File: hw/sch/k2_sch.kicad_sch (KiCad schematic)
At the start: 0 parts

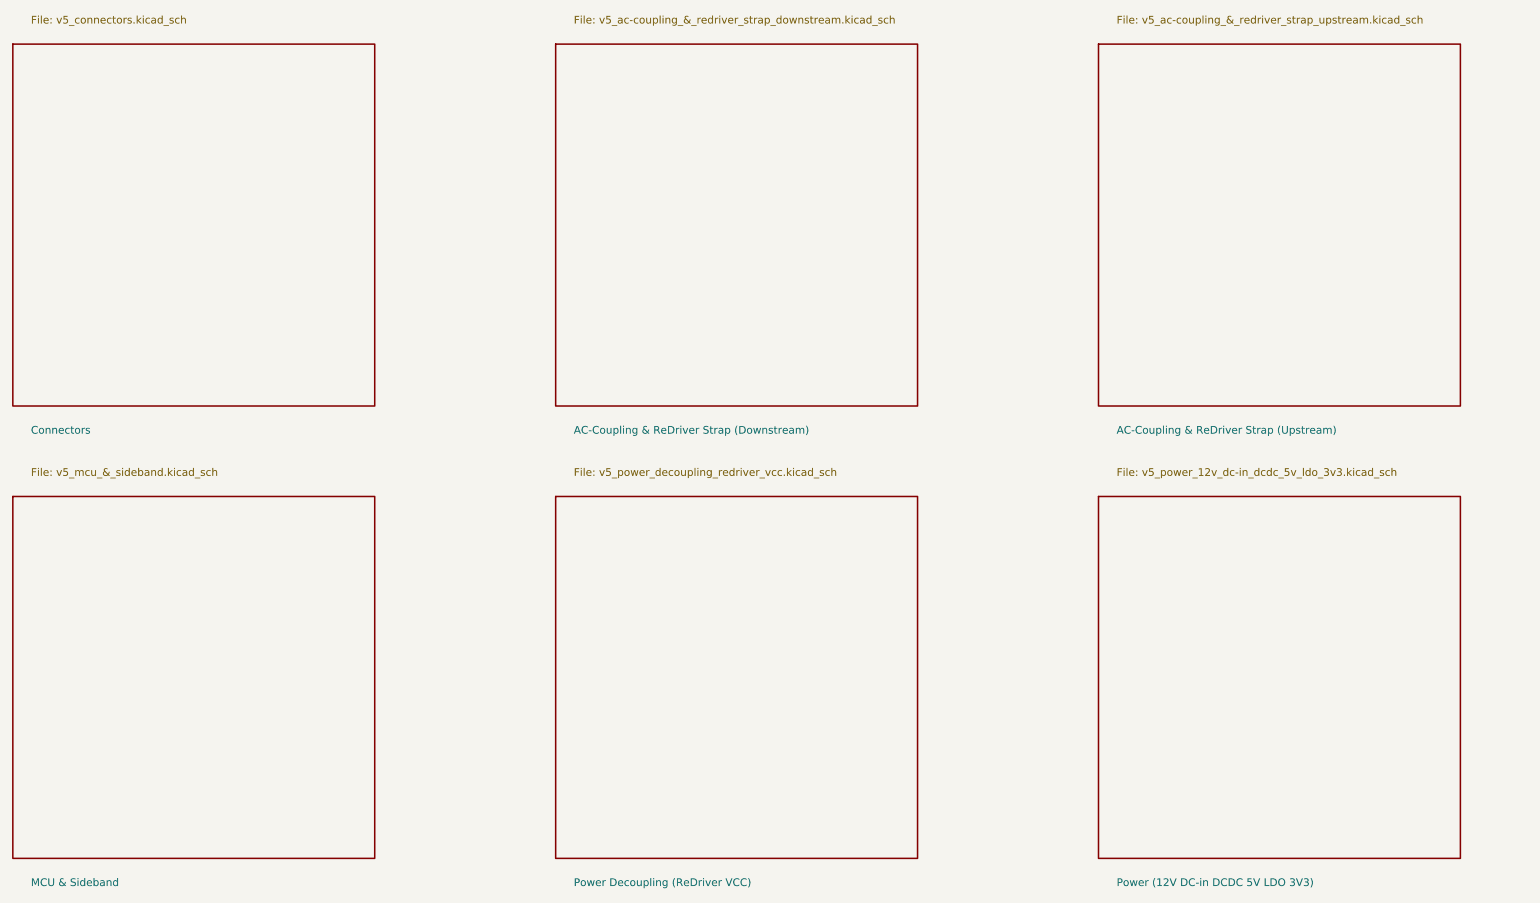
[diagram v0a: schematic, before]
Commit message: p2(k2): #K2-13 五问全落地 —— rev-21 + S2 纸张 A0 + S3 PWR_FLAG + R1/R2 安装 + §五 G1–G8 + E4
一、U1/S1：SPEC rev-21（d46bd017aa560716）
  = rev-20 − anchor_fixes.C64/C66（引 R1 分类留痕：C64=A1 耦合内置 / C66=D 类 VREG 域不存在）
  + spec_version 1.1.spec-rev-21 + _spec_rev_11 溯源卡 + anchor_fixes_removed_v21 留痕。
  机器证明：唯一值变 = spec_version；唯一删除 = C64/C66 六叶子；其余逐字节承 rev-20。
  rev-19/rev-20 原件未改；project.yaml 重指向；L3 README-canonical 同步。

二、S2：k2_sch.yaml 该 sheet paper A2→A0（逐字节 diff 仅 1 行；未采 (b)/(c)）。

三、S3：采纳 (a) —— driver 内 P9 通用规则「有 power_in 且无 power_out 的网各加 1 个虚拟
  PWR_FLAG（in_bom no / on_board no）」，参考号 #FLG01（避免 KiCad 批注错误导出告警）。
  实测命中网 = ['GND']；未改真源引脚类型；(b) 未采用。ERC error = 0。

四、安装（接受重排；原件留档）：写 5 件新 sheet + 覆写 root 与 IOCONVERT.kicad_sym；
  旧 6 件 v5_* 以 git mv 入 hw/sch/archive/（未删）。入 archive/ 系必要处置——判据侧
  measure_sch_refdes() glob 顶层 *.kicad_sch，且 _EXCL 视 /archive/ 为归档，否则 E1 被 6L 旧件污染。
  映射表 + 新 canonical 集合与 sha 见 hw/sch/README-canonical.md（#K2-13 §二.2 禁静默）。

五、落盘后机检
  C1 确定性 PASS（两次连跑逐字节同）
  T1 PASS：退役名 *_U3/_U7 = ∅；32/32 保留名并网且球映射与 T3 表一致
    （PCIe_DN_OUT0_P_MCIO→J3/3 + U6 M26=A_PETP0；UP0_P_J2→J2/2 + U6 P10=B_PETP0）
  T2 留痕：R4/R9/R26/R27 未出现在再生图（真源不含），删据 = 冻结 SPEC strap_domain_v32
    （ALL_DONE/READ_EN = NC no-action）+ R1 C 类；以文档留痕替代编辑级图注（(ii) 不产编辑注）
  E1 复算：板 42 / 图 55 / 网表 55；板-图 = 0；图-板 = 13 = P4 补件（按 O2 登记，非不一致）
  E4 PASS：两次 sha 同（k2_v6.kicad_pcb f615ffe6b83b88a3）+ refs 42 + 边框 120×46mm + 自检 6/6
  ERC：error 0；warning 豁免登记（452 off-grid 真源几何 / 55 lib + 15 footprint 环境 /
    1 lib_symbol_mismatch = PWR_FLAG 内嵌定义）

六、§五 G1–G8 落仓内生成器（k2/tools/k2_gen_v5.py）：板框 46mm、SPEC 经 pm_gate.config（自定位）、
  K2_REFS 由真源板导出、OLD_REF_MAP 与 pad65 特判移除、AC 检查/S7/capacitor_walls 段移除
  （保留 anchor_fixes 严格校验）；E4 判据 + O2 final_target 55 @P4 写入头注。

七、新增：docs/K2-P2-R1R2-LANDING-EVIDENCE-v1.md（本证据包）、
  docs/K2-P4-board-side-defect-register-v1.md（补 13 件 + 7 单节点网 + U6 15 球 C 类防掩）。
  PWR_5V_KEY 按裁定禁删真源（真源保留）；图侧以 no_connect 显式可见，非抹平。
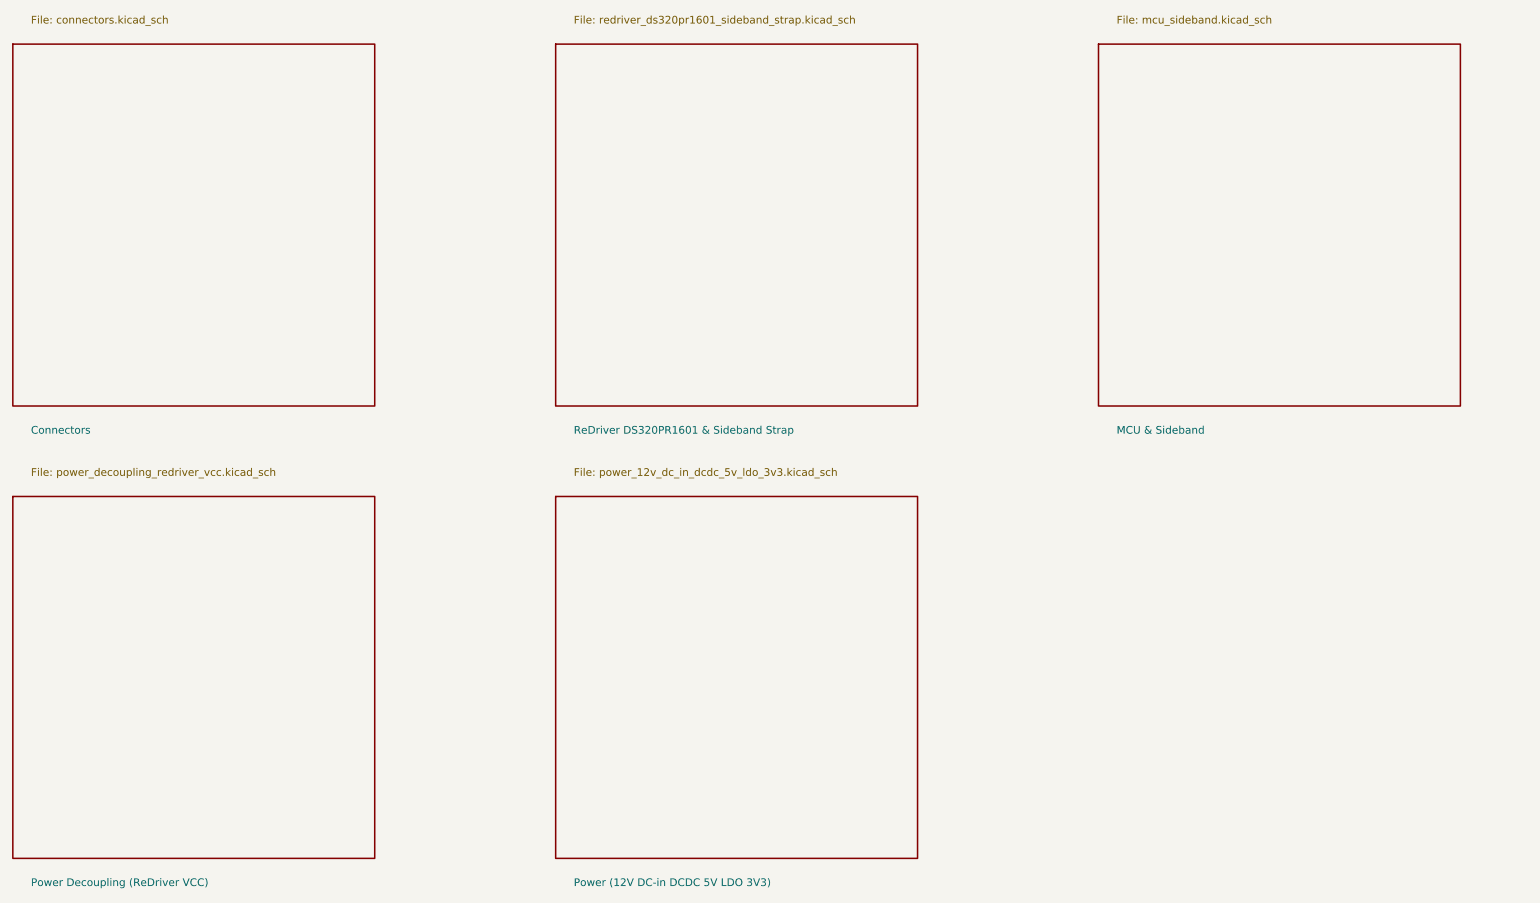
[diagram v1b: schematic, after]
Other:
- removed sheet AC-Coupling & ReDriver Strap (Downstream)
- removed sheet AC-Coupling & ReDriver Strap (Upstream)
- added sheet ReDriver DS320PR1601 & Sideband Strap (redriver_ds320pr1601_sideband_strap.kicad_sch)
- sheet Connectors: file v5_connectors.kicad_sch -> connectors.kicad_sch
- sheet MCU & Sideband: file v5_mcu_&_sideband.kicad_sch -> mcu_sideband.kicad_sch
- sheet Power (12V DC-in DCDC 5V LDO 3V3): file v5_power_12v_dc-in_dcdc_5v_ldo_3v3.kicad_sch -> power_12v_dc_in_dcdc_5v_ldo_3v3.kicad_sch
- sheet Power Decoupling (ReDriver VCC): file v5_power_decoupling_redriver_vcc.kicad_sch -> power_decoupling_redriver_vcc.kicad_sch
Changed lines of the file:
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@@
     (fill (color 0 0 0 0.0000))
     (property "Sheetname" "Connectors" (at 23.000 89.000 0) (effects (font (size 1.27 1.27)) (justify left)))
-    (property "Sheetfile" "v5_connectors.kicad_sch" (at 23.000 21.000 0) (effects (font (size 1.27 1.27)) (justify left)))
+    (property "Sheetfile" "connectors.kicad_sch" (at 23.000 21.000 0) (effects (font (size 1.27 1.27)) (justify left)))
     (instances (project "ioconvert" (path "/9288626a-148d-6529-d53c-cbef0f1380d1" (page "2"))))
   )
@@
     (stroke (width 0.254) (type solid))
     (fill (color 0 0 0 0.0000))
-    (property "Sheetname" "AC-Coupling & ReDriver Strap (Downstream)" (at 113.000 89.000 0) (effects (font (size 1.27 1.27)) (justify left)))
-    (property "Sheetfile" "v5_ac-coupling_&_redriver_strap_downstream.kicad_sch" (at 113.000 21.000 0) (effects (font (size 1.27 1.27)) (justify left)))
-    (instances (project "ioconvert" (path "/37b090a1-0fb6-c2c7-6682-66246403c2c6" (page "3"))))
+    (property "Sheetname" "ReDriver DS320PR1601 & Sideband Strap" (at 113.000 89.000 0) (effects (font (size 1.27 1.27)) (justify left)))
+    (property "Sheetfile" "redriver_ds320pr1601_sideband_strap.kicad_sch" (at 113.000 21.000 0) (effects (font (size 1.27 1.27)) (justify left)))
+    (instances (project "ioconvert" (path "/732bae5b-f232-8e58-95db-01df091e0a6d" (page "3"))))
   )
   (sheet
@@
     (stroke (width 0.254) (type solid))
     (fill (color 0 0 0 0.0000))
-    (property "Sheetname" "AC-Coupling & ReDriver Strap (Upstream)" (at 203.000 89.000 0) (effects (font (size 1.27 1.27)) (justify left)))
-    (property "Sheetfile" "v5_ac-coupling_&_redriver_strap_upstream.kicad_sch" (at 203.000 21.000 0) (effects (font (size 1.27 1.27)) (justify left)))
-    (instances (project "ioconvert" (path "/15353843-f029-fc12-ccb9-4fe8fc7a5228" (page "4"))))
+    (property "Sheetname" "MCU & Sideband" (at 203.000 89.000 0) (effects (font (size 1.27 1.27)) (justify left)))
+    (property "Sheetfile" "mcu_sideband.kicad_sch" (at 203.000 21.000 0) (effects (font (size 1.27 1.27)) (justify left)))
+    (instances (project "ioconvert" (path "/7d4441b6-df64-f74b-c7d2-677325e3aa18" (page "4"))))
   )
   (sheet
@@
     (stroke (width 0.254) (type solid))
     (fill (color 0 0 0 0.0000))
-    (property "Sheetname" "MCU & Sideband" (at 23.000 164.000 0) (effects (font (size 1.27 1.27)) (justify left)))
-    (property "Sheetfile" "v5_mcu_&_sideband.kicad_sch" (at 23.000 96.000 0) (effects (font (size 1.27 1.27)) (justify left)))
-    (instances (project "ioconvert" (path "/7d4441b6-df64-f74b-c7d2-677325e3aa18" (page "5"))))
+    (property "Sheetname" "Power Decoupling (ReDriver VCC)" (at 23.000 164.000 0) (effects (font (size 1.27 1.27)) (justify left)))
+    (property "Sheetfile" "power_decoupling_redriver_vcc.kicad_sch" (at 23.000 96.000 0) (effects (font (size 1.27 1.27)) (justify left)))
+    (instances (project "ioconvert" (path "/8339d47c-c730-a0fb-106c-c9e37ad45feb" (page "5"))))
   )
   (sheet
@@
     (stroke (width 0.254) (type solid))
     (fill (color 0 0 0 0.0000))
-    (property "Sheetname" "Power Decoupling (ReDriver VCC)" (at 113.000 164.000 0) (effects (font (size 1.27 1.27)) (justify left)))
-    (property "Sheetfile" "v5_power_decoupling_redriver_vcc.kicad_sch" (at 113.000 96.000 0) (effects (font (size 1.27 1.27)) (justify left)))
-    (instances (project "ioconvert" (path "/8339d47c-c730-a0fb-106c-c9e37ad45feb" (page "6"))))
-  )
-  (sheet
-    (at 200.000 100.000)
-    (size 60.000 60.000)
-    (fields_autoplaced yes)
-    (stroke (width 0.254) (type solid))
-    (fill (color 0 0 0 0.0000))
-    (property "Sheetname" "Power (12V DC-in DCDC 5V LDO 3V3)" (at 203.000 164.000 0) (effects (font (size 1.27 1.27)) (justify left)))
-    (property "Sheetfile" "v5_power_12v_dc-in_dcdc_5v_ldo_3v3.kicad_sch" (at 203.000 96.000 0) (effects (font (size 1.27 1.27)) (justify left)))
-    (instances (project "ioconvert" (path "/76204242-bcfb-1e6c-8fe9-63ec820c686c" (page "7"))))
+    (property "Sheetname" "Power (12V DC-in DCDC 5V LDO 3V3)" (at 113.000 164.000 0) (effects (font (size 1.27 1.27)) (justify left)))
+    (property "Sheetfile" "power_12v_dc_in_dcdc_5v_ldo_3v3.kicad_sch" (at 113.000 96.000 0) (effects (font (size 1.27 1.27)) (justify left)))
+    (instances (project "ioconvert" (path "/76204242-bcfb-1e6c-8fe9-63ec820c686c" (page "6"))))
   )
   (sheet_instances
     (path "/" (page "1"))
     (path "/9288626a-148d-6529-d53c-cbef0f1380d1" (page "2"))
-    (path "/37b090a1-0fb6-c2c7-6682-66246403c2c6" (page "3"))
-    (path "/15353843-f029-fc12-ccb9-4fe8fc7a5228" (page "4"))
-    (path "/7d4441b6-df64-f74b-c7d2-677325e3aa18" (page "5"))
-    (path "/8339d47c-c730-a0fb-106c-c9e37ad45feb" (page "6"))
-    (path "/76204242-bcfb-1e6c-8fe9-63ec820c686c" (page "7"))
+    (path "/732bae5b-f232-8e58-95db-01df091e0a6d" (page "3"))
+    (path "/7d4441b6-df64-f74b-c7d2-677325e3aa18" (page "4"))
+    (path "/8339d47c-c730-a0fb-106c-c9e37ad45feb" (page "5"))
+    (path "/76204242-bcfb-1e6c-8fe9-63ec820c686c" (page "6"))
   )
 )
